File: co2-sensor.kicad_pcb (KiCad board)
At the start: 2 copper layers, 92.5 x 70.5 mm, 51 parts, among them J1 Waveshare E-Ink, J2 USB-C Receptacle, J3 JST 2-PH, Q2 AO3400A, Q3 DMP2045U, SW1 SW_Push, SW2 SW_Push, SW3 SW_Push, SW4 SW_Push, SW5 SW_Push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

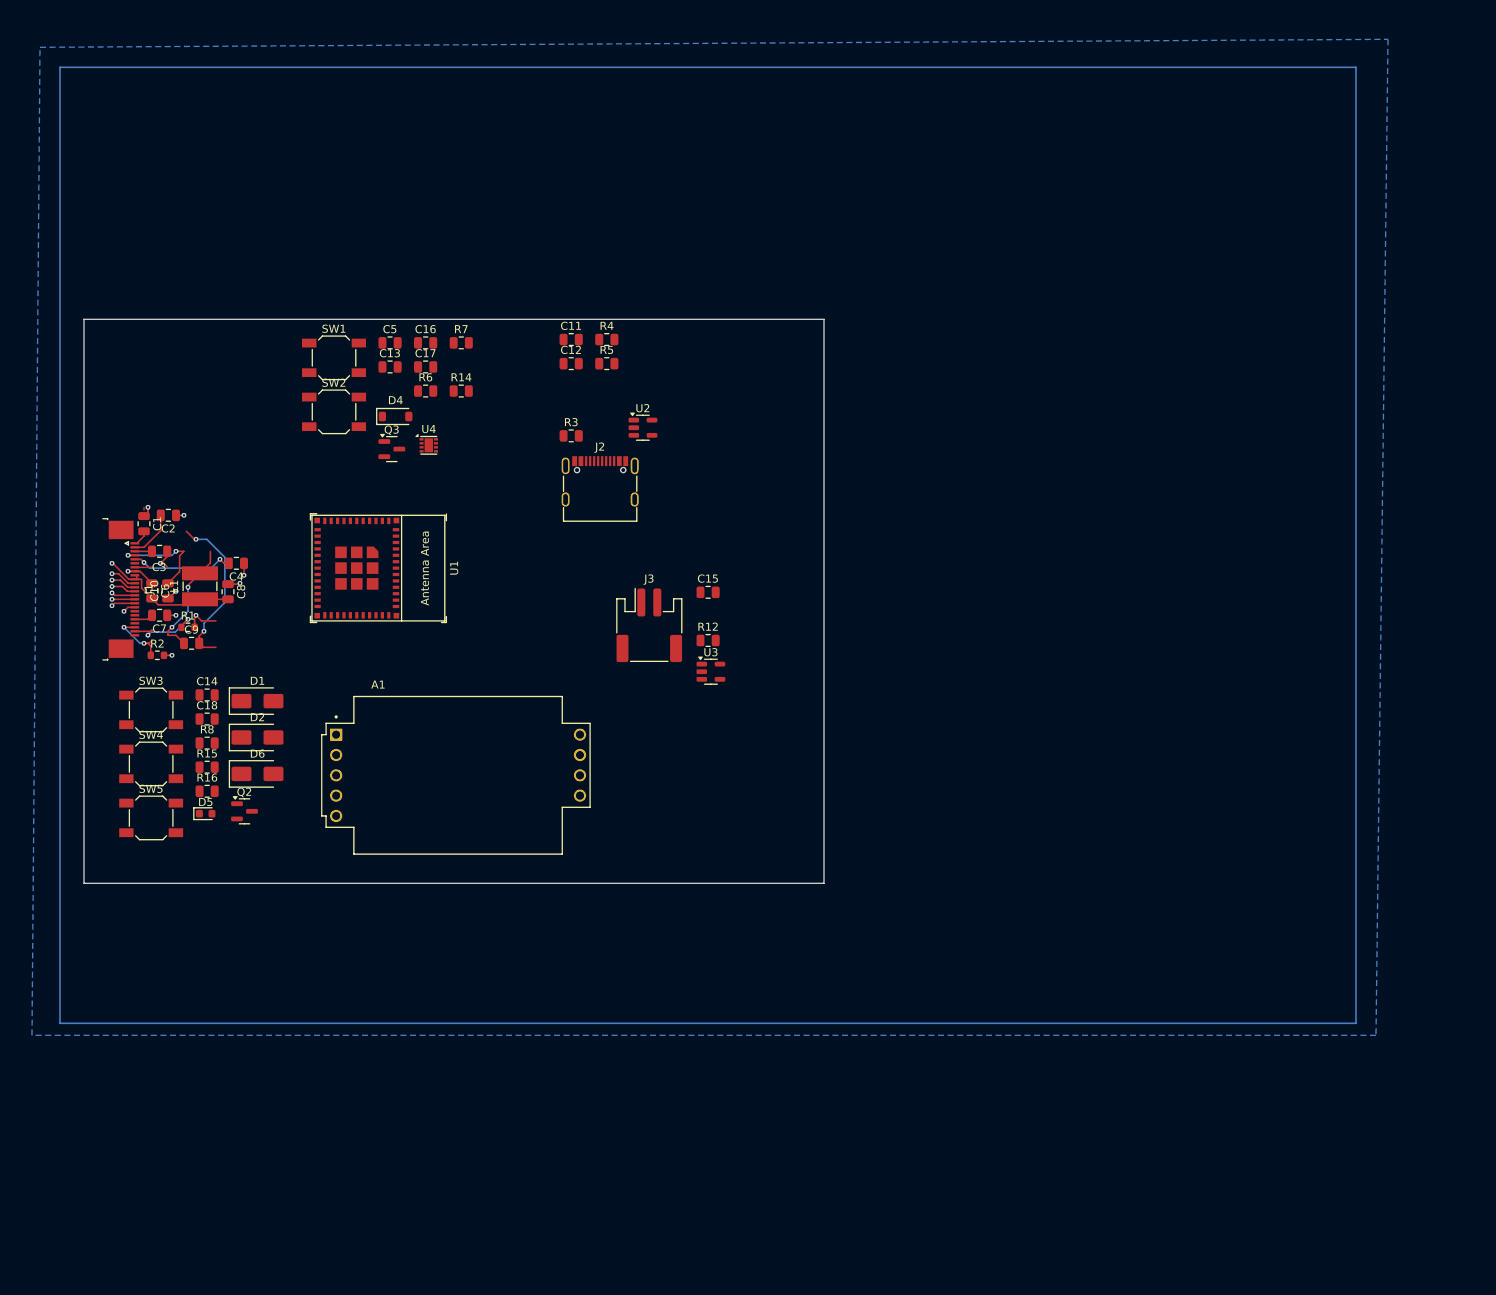
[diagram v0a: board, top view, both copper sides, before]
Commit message: Add all LCSC part numbers
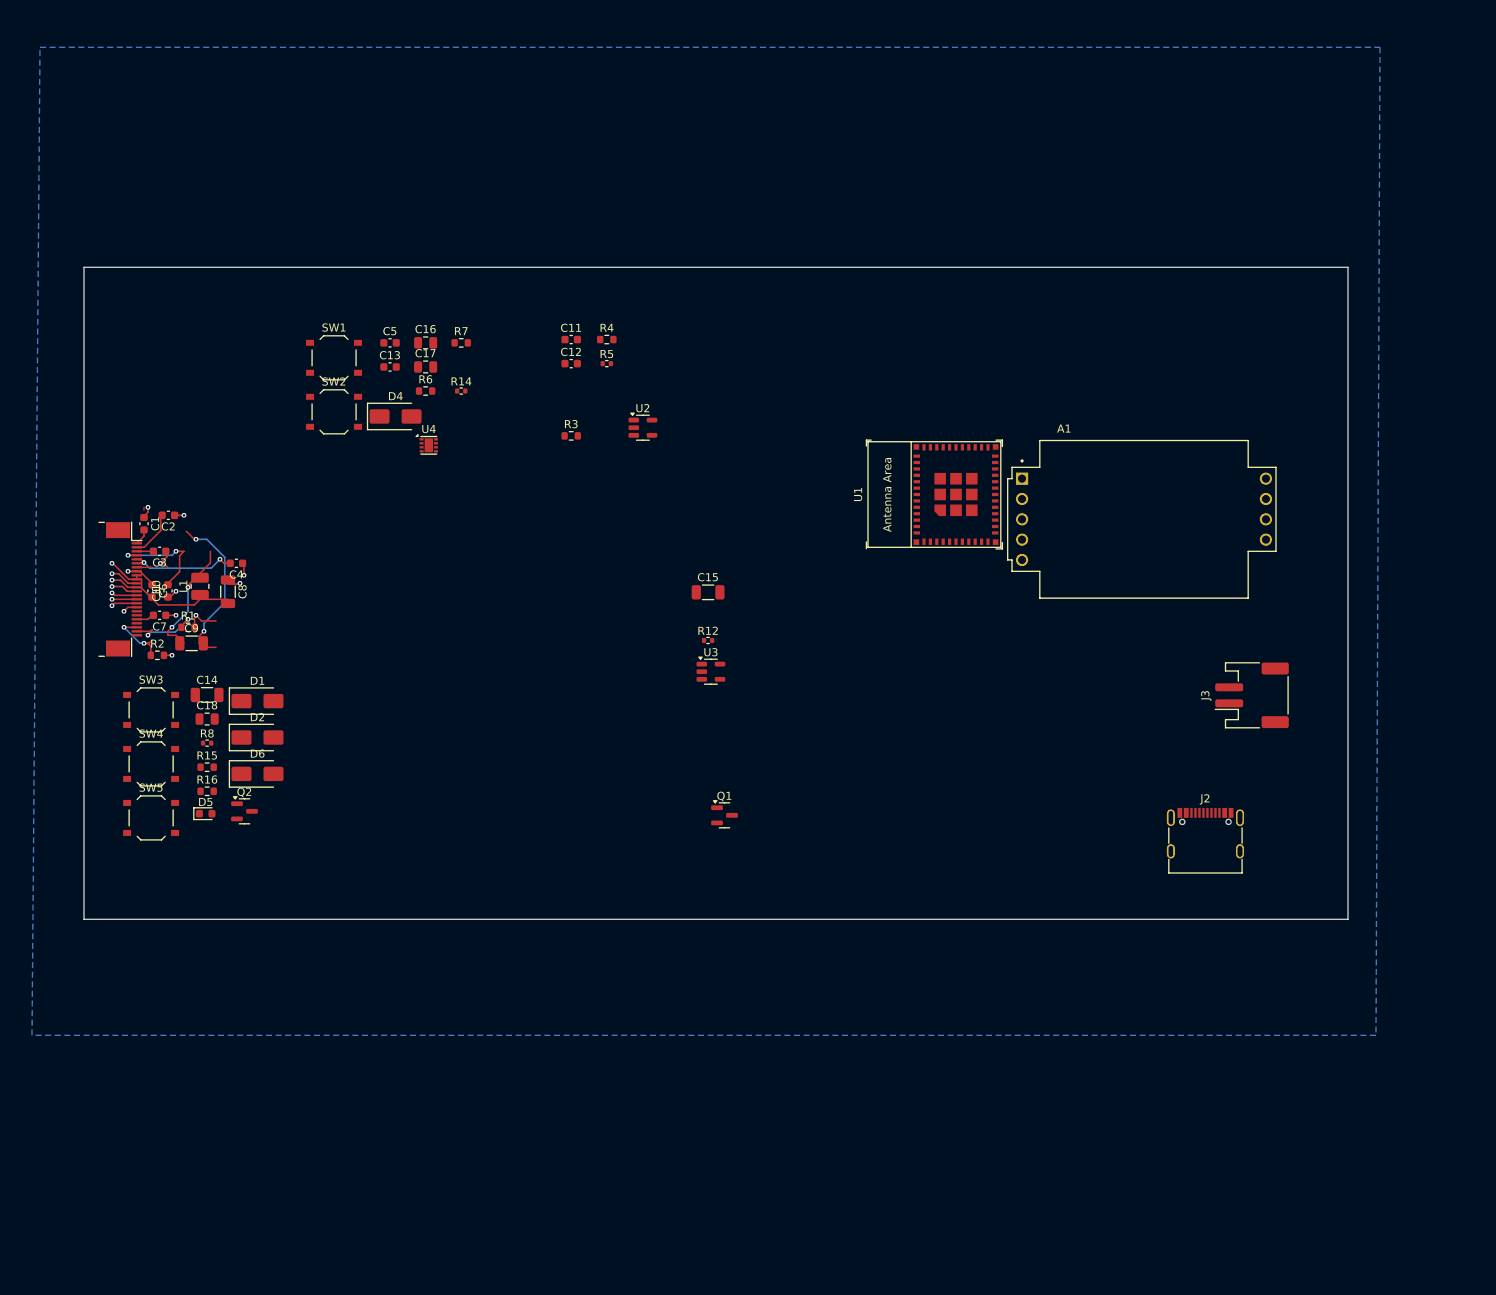
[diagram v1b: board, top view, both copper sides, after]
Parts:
- removed Q3: DMP2045U, Package_TO_SOT_SMD:SOT-23
- added Q1: AO3401A, Package_TO_SOT_SMD:SOT-23, F.Cu at (113.6, 134.5)
- C1, C10, C11, C12, C13, C2, C3, C4, C5, C6, C7: footprint Capacitor_SMD:C_0805_2012Metric -> Capacitor_SMD:C_0603_1608Metric
- C14, C15, C8, C9: footprint Capacitor_SMD:C_0805_2012Metric -> Capacitor_SMD:C_1206_3216Metric
- D4: footprint Diode_SMD:D_SOD-123 -> Diode_SMD:D_SMA
- J1: value Waveshare E-Ink -> 24P FPC Connector; footprint Connector_FFC-FPC:TE_2-1734839-4_1x24-1MP_P0.5mm_Horizontal -> Connector_FFC-FPC:Jushuo_AFC07-S24FCA-00_1x24-1MP_P0.50_Horizontal
- L1: footprint Inductor_SMD:L_Ferrocore_DLG-0403 -> Inductor_SMD:L_1008_2520Metric
- R12, R14, R5, R8: footprint Capacitor_SMD:C_0805_2012Metric -> Resistor_SMD:R_0402_1005Metric
- R15, R16, R3, R4, R6, R7: footprint Capacitor_SMD:C_0805_2012Metric -> Resistor_SMD:R_0603_1608Metric
- R2: value 2Ω -> 2.2Ω
- SW1, SW2, SW3, SW4, SW5: footprint Button_Switch_SMD:SW_SPST_SKQG_WithStem -> Button_Switch_SMD:SW_Push_1P1T_XKB_TS-1187A
- moved A1 91.5 mm to (166.0, 97.5)
- moved J2 87.5 mm to (173.7, 137.9)
- moved J3 75.8 mm to (179.5, 119.5), turned to 90 degrees
- moved U1 70.1 mm to (139.8, 94.4), turned to 90 degrees
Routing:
- net +3.3V: track 18.1 -> 23.9 mm, vias 1 -> 3
- net /EINK_CS: track 3.10 -> 0.00 mm, vias 1 -> 0
- net /EINK_SCLK: track 3.22 -> 6.32 mm, vias 1 -> 2
- net /EINK_MOSI: track 3.35 -> 6.32 mm, vias 1 -> 2
- net /EINK_DC: track 2.97 -> 0.00 mm, vias 1 -> 0
- net /EINK_BUSY: track 2.97 -> 0.00 mm, vias 1 -> 0
- net /EINK_RES: track 2.85 -> 0.00 mm, vias 1 -> 0
- net unconnected-(J1-Pin_7-Pad7): track 0.00 -> 2.20 mm
- net Net-(J1-Pin_18): track 2.20 -> 0.00 mm
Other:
- board size 92.5 x 70.5 mm -> 158 x 81.5 mm

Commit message: Move components around
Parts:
- A1: moved to B.Cu
- D1, D2, D4, D6: footprint Diode_SMD:D_SMA -> Diode_SMD:D_SOD-123
- J1: value 24P FPC Connector -> 24-pin FPC Connector
- moved C18 127.9 mm to (175.0, 144.1), turned to 90 degrees
- moved C14 127.0 mm to (175.0, 134.5), turned to -90 degrees
- moved R8 120.6 mm to (169.0, 136.5), turned to 180 degrees
- moved D5 120.3 mm to (169.0, 134.0), turned to 90 degrees
- moved R2 115.0 mm to (157.5, 108.0), turned to 90 degrees
- moved D4 114.2 mm to (180.0, 123.0)
- moved R1 113.0 mm to (159.5, 108.0), turned to 90 degrees
- moved L1 111.1 mm to (158.5, 116.9)
- moved U4 111.0 mm to (172.5, 144.1), turned to 180 degrees
- moved C8 110.4 mm to (161.5, 116.0)
- moved C10 107.7 mm to (151.2, 116.5), turned to 0 degrees
- moved C1 107.6 mm to (147.5, 113.5), turned to 180 degrees
- moved Q2 107.3 mm to (158.6, 111.9), turned to -90 degrees
- moved C6 105.5 mm to (147.5, 104.5), turned to 180 degrees
- moved R14 105.5 mm to (173.0, 132.5)
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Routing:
- net +3.3V: track 23.9 -> 0.00 mm, vias 3 -> 0
- net GND: track 21.6 -> 0.00 mm, vias 11 -> 0
- net Net-(D1-A): track 20.5 -> 0.00 mm, vias 2 -> 0
- net Net-(D2-A): track 15.1 -> 0.00 mm, vias 2 -> 0
- net /PREVGH: track 13.1 -> 0.00 mm, vias 2 -> 0
- net Net-(J1-Pin_20): track 12.9 -> 0.00 mm, vias 2 -> 0
- net /GDR: track 9.98 -> 0.00 mm, vias 2 -> 0
- net /RESE: track 8.22 -> 0.00 mm, vias 2 -> 0
- net /EINK_MOSI: track 6.32 -> 0.00 mm, vias 2 -> 0
- net /EINK_SCLK: track 6.32 -> 0.00 mm, vias 2 -> 0
- net /PREVGL: track 5.77 -> 0.00 mm
- net unconnected-(J1-Pin_7-Pad7): track 2.20 -> 0.00 mm
- net Net-(J1-Pin_5): track 2.11 -> 0.00 mm
- net /VCOM: track 1.97 -> 0.00 mm
- net Net-(J1-Pin_22): track 1.90 -> 0.00 mm
- added copper zone on F.Cu, net GND
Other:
- board size 158 x 81.5 mm -> 47 x 81.5 mm

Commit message: Move around some more
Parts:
- A1: moved to F.Cu
- moved C16 56.5 mm to (120.0, 75.6), turned to -90 degrees
- moved C14 54.4 mm to (185.0, 81.0)
- moved C15 54.4 mm to (182.5, 85.0)
- moved D5 54.4 mm to (179.0, 80.5)
- moved R12 54.4 mm to (181.0, 78.0)
- moved R14 54.4 mm to (183.0, 79.0)
- moved R8 54.4 mm to (179.0, 83.0)
- moved U3 54.4 mm to (182.0, 81.5)
- moved C18 53.0 mm to (177.5, 91.1), turned to 0 degrees
- moved C17 52.2 mm to (118.5, 79.6), turned to -90 degrees
- moved U4 50.7 mm to (177.5, 93.6)
- moved C12 50.5 mm to (179.5, 74.0)
- moved R5 50.5 mm to (182.2, 71.0)
- moved C11 50.5 mm to (182.3, 73.7)
- moved U2 50.5 mm to (179.4, 71.5)
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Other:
- board size 47 x 81.5 mm -> 60 x 60 mm

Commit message: Don't know?
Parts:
- removed D4: SS14, Diode_SMD:D_SOD-123
- added D3: B5819W, Diode_SMD:D_SOD-123, F.Cu at (185.5, 71.0)
- D1, D2, D6: value SS14 -> B5819W
- SW1, SW2, SW3, SW4, SW5: footprint Button_Switch_SMD:SW_Push_1P1T_XKB_TS-1187A -> footprints:TS24CA
- moved J1 54.5 mm to (181.8, 116.9), turned to 90 degrees
- moved C2 38.9 mm to (173.7, 121.0), turned to 0 degrees
- moved C1 38.8 mm to (173.7, 125.0), turned to 0 degrees
- moved C5 38.8 mm to (173.7, 123.5), turned to 0 degrees
- moved C3 38.7 mm to (173.7, 118.5), turned to 0 degrees
- moved C4 38.7 mm to (173.7, 117.0), turned to 0 degrees
- moved C6 38.7 mm to (173.7, 115.5), turned to 0 degrees
- moved C7 38.7 mm to (173.7, 111.0), turned to 0 degrees
- moved D1 29.8 mm to (164.3, 129.0), turned to 180 degrees
- moved D6 29.6 mm to (164.3, 126.5), turned to 0 degrees
- moved C10 26.9 mm to (166.0, 118.5), turned to 180 degrees
- moved SW5 24.5 mm to (120.8, 152.4), turned to 0 degrees
- moved D2 19.4 mm to (161.3, 118.5), turned to 180 degrees
- moved C9 18.9 mm to (159.0, 126.5), turned to 0 degrees
- moved R2 16.3 mm to (161.5, 110.0), turned to 180 degrees
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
